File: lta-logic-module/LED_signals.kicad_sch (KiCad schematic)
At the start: 12 parts, among them J3 Conn_01x12, J4 Conn_01x12, U10 SN74LVC00AD, U6 SN74LVC00AD, U7 SN74LVC00AD, U9 SN74LVC00AD

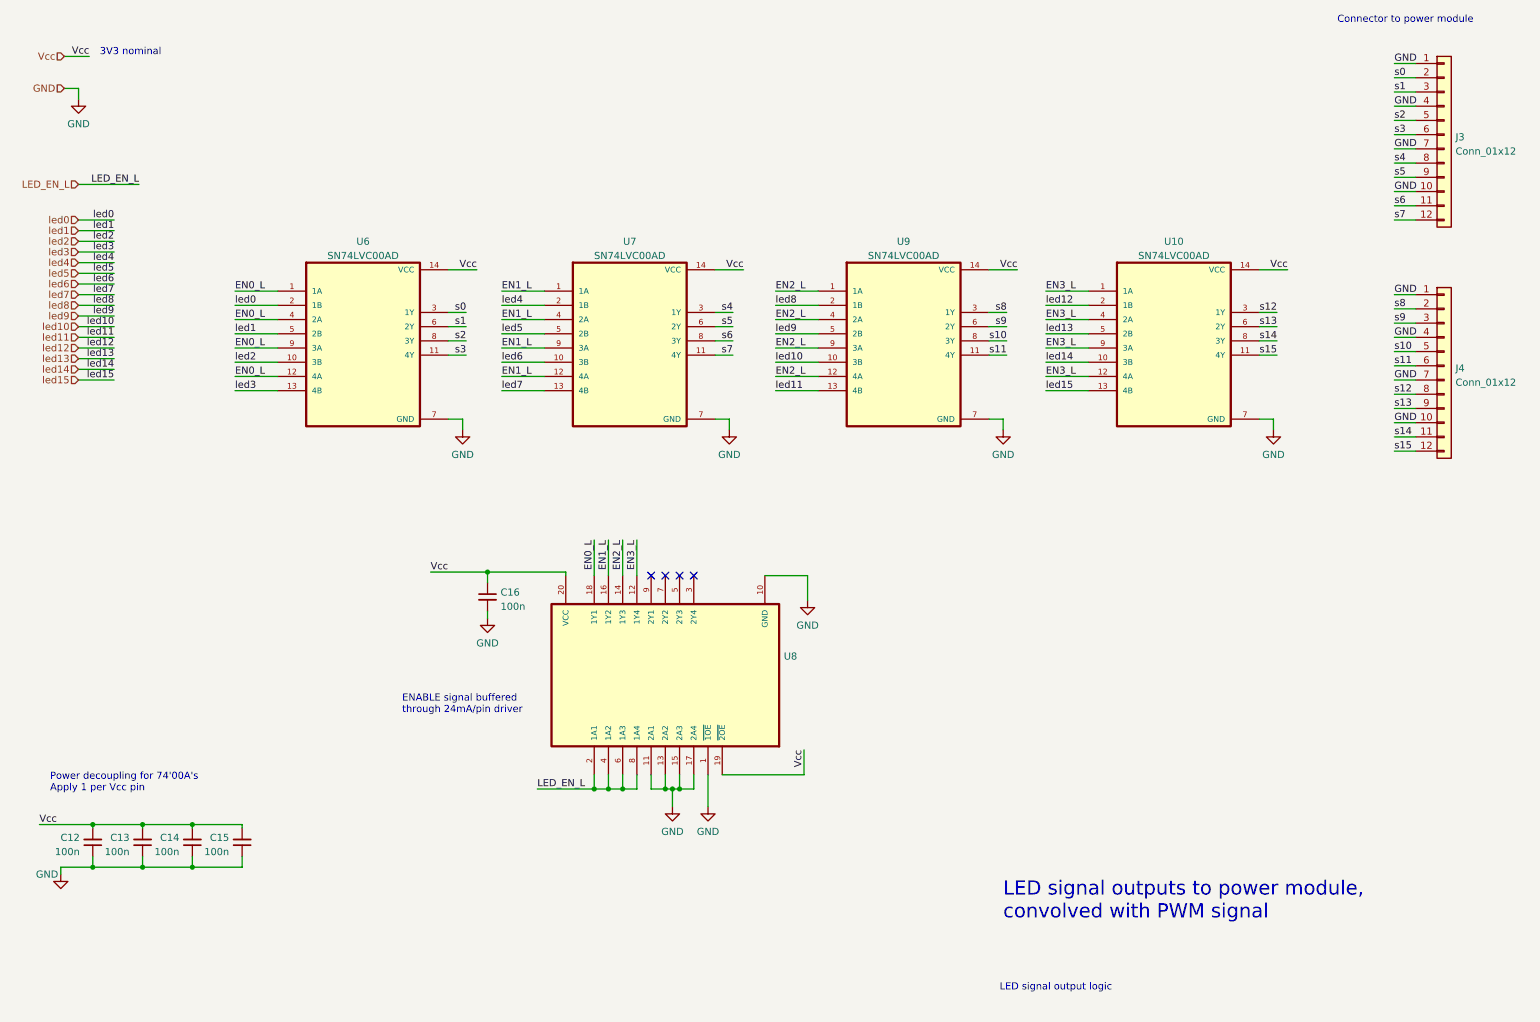
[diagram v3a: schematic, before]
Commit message: Add light sensor circuit.
Adjust TODOs and comments after testing btn circuit.
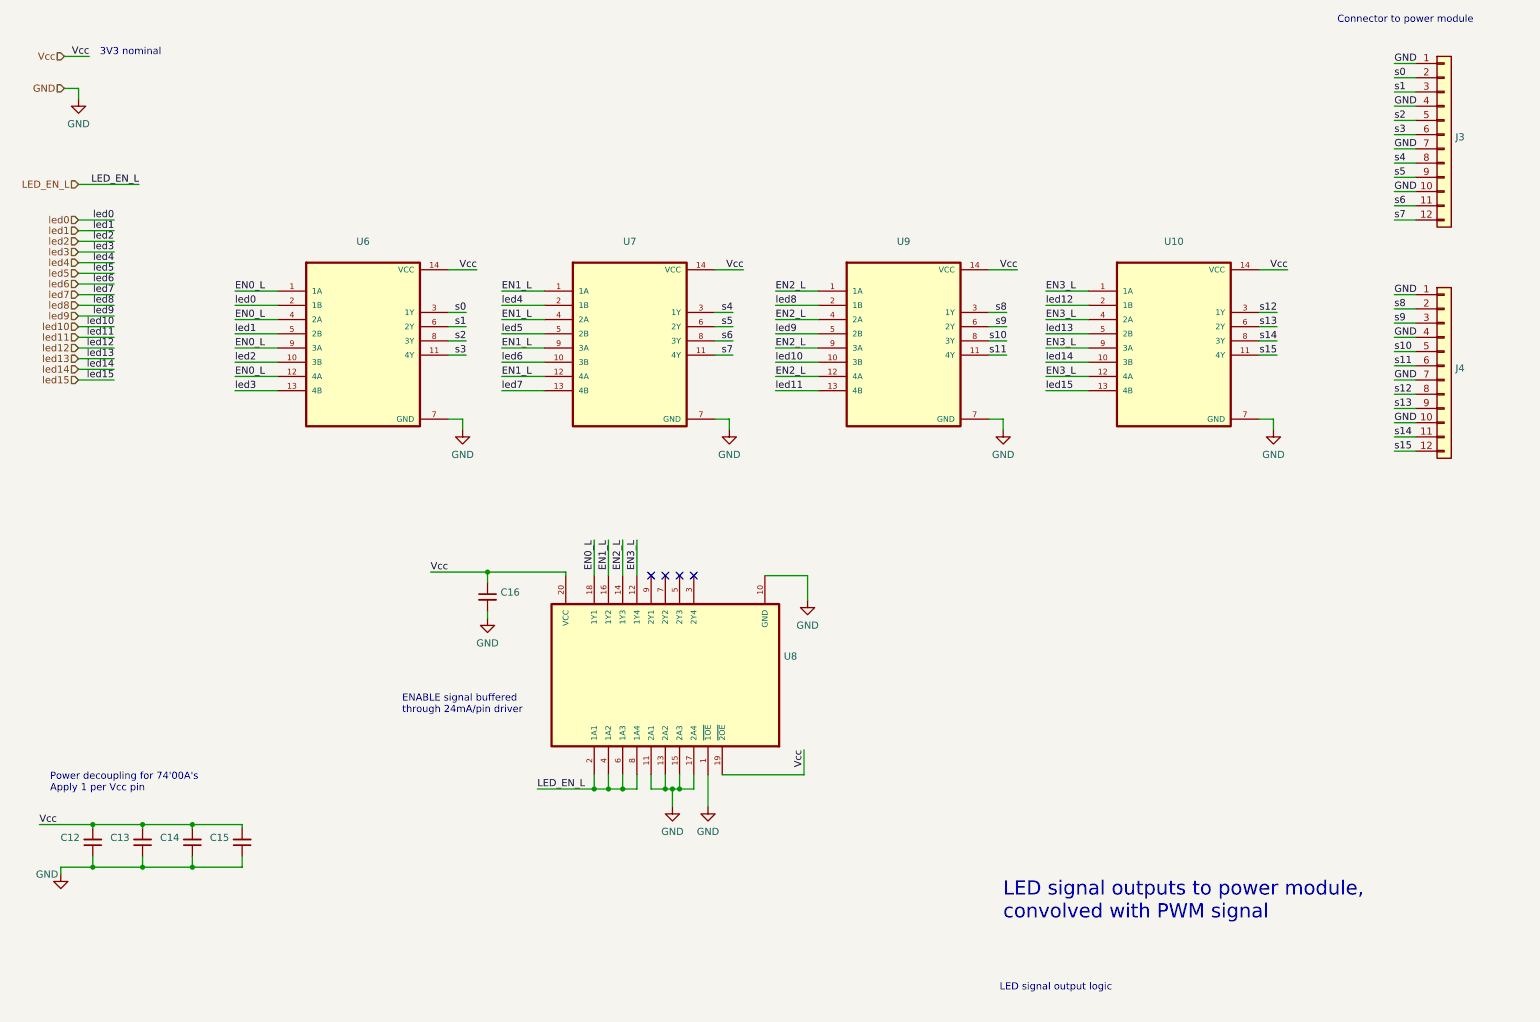
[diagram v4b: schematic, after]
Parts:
- C12, C13, C14, C15, C16: value 100n -> (none); footprint Capacitor_SMD:C_0603_1608Metric -> (none)
- J3, J4: value Conn_01x12 -> (none); footprint Connector_PinHeader_2.54mm:PinHeader_1x12_P2.54mm_Vertical -> (none)
- U10, U6, U7, U9: value SN74LVC00AD -> (none); footprint Aaron_TI_Parts:TI_SOIC_D_R-PDSO-G14 -> (none)
- U8: footprint Aaron_TI_Parts:TI_SOIC_DW0020A -> (none)
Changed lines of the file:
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@@
       (effects (font (size 1.27 1.27)) (justify right))
     )
-    (property "Value" "100n" (id 1) (at 26.2509 165.5258 0)
-      (effects (font (size 1.27 1.27)) (justify right))
-    )
-    (property "Footprint" "Capacitor_SMD:C_0603_1608Metric" (id 2) (at 28.575 163.83 0)
+    (property "Value" "" (id 1) (at 26.2509 165.5258 0)
+      (effects (font (size 1.27 1.27)) (justify right))
+    )
+    (property "Footprint" "" (id 2) (at 28.575 163.83 0)
       (effects (font (size 1.27 1.27)) hide)
     )
@@
   (symbol (lib_id "power:GND") (at 191.135 90.17 0) (unit 1)
     (in_bom yes) (on_board yes) (fields_autoplaced)
-    (property "Reference" "#PWR040" (id 0) (at 191.135 96.52 0)
+    (property "Reference" "#PWR042" (id 0) (at 191.135 96.52 0)
       (effects (font (size 1.27 1.27)) hide)
     )
@@
     (in_bom yes) (on_board yes) (fields_autoplaced)
     (property "Reference" "U6" (id 0) (at 76.835 56.549 0))
-    (property "Value" "SN74LVC00AD" (id 1) (at 76.835 59.0859 0))
-    (property "Footprint" "Aaron_TI_Parts:TI_SOIC_D_R-PDSO-G14" (id 2) (at 74.295 80.645 0)
+    (property "Value" "" (id 1) (at 76.835 59.0859 0))
+    (property "Footprint" "" (id 2) (at 74.295 80.645 0)
       (effects (font (size 1.27 1.27)) (justify left bottom) hide)
     )
@@
       (effects (font (size 1.27 1.27)) (justify right))
     )
-    (property "Value" "100n" (id 1) (at 52.9209 165.5258 0)
-      (effects (font (size 1.27 1.27)) (justify right))
-    )
-    (property "Footprint" "Capacitor_SMD:C_0603_1608Metric" (id 2) (at 55.245 163.83 0)
+    (property "Value" "" (id 1) (at 52.9209 165.5258 0)
+      (effects (font (size 1.27 1.27)) (justify right))
+    )
+    (property "Footprint" "" (id 2) (at 55.245 163.83 0)
       (effects (font (size 1.27 1.27)) hide)
     )
@@
       (effects (font (size 1.27 1.27)) (justify left))
     )
-    (property "Value" "Conn_01x12" (id 1) (at 271.907 40.4372 0)
-      (effects (font (size 1.27 1.27)) (justify left))
-    )
-    (property "Footprint" "Connector_PinHeader_2.54mm:PinHeader_1x12_P2.54mm_Vertical" (id 2) (at 269.875 37.465 0)
+    (property "Value" "" (id 1) (at 271.907 40.4372 0)
+      (effects (font (size 1.27 1.27)) (justify left))
+    )
+    (property "Footprint" "" (id 2) (at 269.875 37.465 0)
       (effects (font (size 1.27 1.27)) hide)
     )
@@
     (in_bom yes) (on_board yes) (fields_autoplaced)
     (property "Reference" "U10" (id 0) (at 221.615 56.549 0))
-    (property "Value" "SN74LVC00AD" (id 1) (at 221.615 59.0859 0))
-    (property "Footprint" "Aaron_TI_Parts:TI_SOIC_D_R-PDSO-G14" (id 2) (at 219.075 80.645 0)
+    (property "Value" "" (id 1) (at 221.615 59.0859 0))
+    (property "Footprint" "" (id 2) (at 219.075 80.645 0)
       (effects (font (size 1.27 1.27)) (justify left bottom) hide)
     )
@@
   (symbol (lib_id "power:GND") (at 22.86 169.545 0) (unit 1)
     (in_bom yes) (on_board yes)
-    (property "Reference" "#PWR032" (id 0) (at 22.86 175.895 0)
+    (property "Reference" "#PWR034" (id 0) (at 22.86 175.895 0)
       (effects (font (size 1.27 1.27)) hide)
     )
@@
   (symbol (lib_id "power:GND") (at 239.395 90.17 0) (unit 1)
     (in_bom yes) (on_board yes) (fields_autoplaced)
-    (property "Reference" "#PWR041" (id 0) (at 239.395 96.52 0)
+    (property "Reference" "#PWR043" (id 0) (at 239.395 96.52 0)
       (effects (font (size 1.27 1.27)) hide)
     )
@@
       (effects (font (size 1.27 1.27)) (justify left))
     )
-    (property "Value" "100n" (id 1) (at 101.3841 121.7235 0)
-      (effects (font (size 1.27 1.27)) (justify left))
-    )
-    (property "Footprint" "Capacitor_SMD:C_0603_1608Metric" (id 2) (at 99.06 120.015 0)
+    (property "Value" "" (id 1) (at 101.3841 121.7235 0)
+      (effects (font (size 1.27 1.27)) (justify left))
+    )
+    (property "Footprint" "" (id 2) (at 99.06 120.015 0)
       (effects (font (size 1.27 1.27)) hide)
     )
@@
       (effects (font (size 1.27 1.27)) (justify right))
     )
-    (property "Value" "100n" (id 1) (at 35.1409 165.5258 0)
-      (effects (font (size 1.27 1.27)) (justify right))
-    )
-    (property "Footprint" "Capacitor_SMD:C_0603_1608Metric" (id 2) (at 37.465 163.83 0)
+    (property "Value" "" (id 1) (at 35.1409 165.5258 0)
+      (effects (font (size 1.27 1.27)) (justify right))
+    )
+    (property "Footprint" "" (id 2) (at 37.465 163.83 0)
       (effects (font (size 1.27 1.27)) hide)
     )
@@
     (in_bom yes) (on_board yes) (fields_autoplaced)
     (property "Reference" "U7" (id 0) (at 124.46 56.549 0))
-    (property "Value" "SN74LVC00AD" (id 1) (at 124.46 59.0859 0))
-    (property "Footprint" "Aaron_TI_Parts:TI_SOIC_D_R-PDSO-G14" (id 2) (at 121.92 80.645 0)
+    (property "Value" "" (id 1) (at 124.46 59.0859 0))
+    (property "Footprint" "" (id 2) (at 121.92 80.645 0)
       (effects (font (size 1.27 1.27)) (justify left bottom) hide)
     )
@@
       (effects (font (size 1.27 1.27)) (justify right))
     )
-    (property "Footprint" "Aaron_TI_Parts:TI_SOIC_DW0020A" (id 2) (at 130.81 133.985 0)
+    (property "Footprint" "" (id 2) (at 130.81 133.985 0)
       (effects (font (size 1.27 1.27)) (justify left bottom) hide)
     )
@@
   (symbol (lib_id "power:GND") (at 156.21 120.65 0) (unit 1)
     (in_bom yes) (on_board yes) (fields_autoplaced)
-    (property "Reference" "#PWR039" (id 0) (at 156.21 127 0)
+    (property "Reference" "#PWR041" (id 0) (at 156.21 127 0)
       (effects (font (size 1.27 1.27)) hide)
     )
@@
   (symbol (lib_id "power:GND") (at 99.06 123.825 0) (unit 1)
     (in_bom yes) (on_board yes) (fields_autoplaced)
-    (property "Reference" "#PWR035" (id 0) (at 99.06 130.175 0)
+    (property "Reference" "#PWR037" (id 0) (at 99.06 130.175 0)
       (effects (font (size 1.27 1.27)) hide)
     )
@@
   (symbol (lib_id "power:GND") (at 142.24 90.17 0) (unit 1)
     (in_bom yes) (on_board yes) (fields_autoplaced)
-    (property "Reference" "#PWR038" (id 0) (at 142.24 96.52 0)
+    (property "Reference" "#PWR040" (id 0) (at 142.24 96.52 0)
       (effects (font (size 1.27 1.27)) hide)
     )
@@
       (effects (font (size 1.27 1.27)) (justify right))
     )
-    (property "Value" "100n" (id 1) (at 44.0309 165.5258 0)
-      (effects (font (size 1.27 1.27)) (justify right))
-    )
-    (property "Footprint" "Capacitor_SMD:C_0603_1608Metric" (id 2) (at 46.355 163.83 0)
+    (property "Value" "" (id 1) (at 44.0309 165.5258 0)
+      (effects (font (size 1.27 1.27)) (justify right))
+    )
+    (property "Footprint" "" (id 2) (at 46.355 163.83 0)
       (effects (font (size 1.27 1.27)) hide)
     )
@@
   (symbol (lib_id "power:GND") (at 132.08 157.48 0) (unit 1)
     (in_bom yes) (on_board yes) (fields_autoplaced)
-    (property "Reference" "#PWR036" (id 0) (at 132.08 163.83 0)
+    (property "Reference" "#PWR038" (id 0) (at 132.08 163.83 0)
       (effects (font (size 1.27 1.27)) hide)
     )
@@
   (symbol (lib_id "power:GND") (at 138.43 157.48 0) (unit 1)
     (in_bom yes) (on_board yes) (fields_autoplaced)
-    (property "Reference" "#PWR037" (id 0) (at 138.43 163.83 0)
+    (property "Reference" "#PWR039" (id 0) (at 138.43 163.83 0)
       (effects (font (size 1.27 1.27)) hide)
     )
@@
     (in_bom yes) (on_board yes) (fields_autoplaced)
     (property "Reference" "U9" (id 0) (at 173.355 56.549 0))
-    (property "Value" "SN74LVC00AD" (id 1) (at 173.355 59.0859 0))
-    (property "Footprint" "Aaron_TI_Parts:TI_SOIC_D_R-PDSO-G14" (id 2) (at 170.815 80.645 0)
+    (property "Value" "" (id 1) (at 173.355 59.0859 0))
+    (property "Footprint" "" (id 2) (at 170.815 80.645 0)
       (effects (font (size 1.27 1.27)) (justify left bottom) hide)
     )
@@
   (symbol (lib_id "power:GND") (at 26.035 31.115 0) (unit 1)
     (in_bom yes) (on_board yes) (fields_autoplaced)
-    (property "Reference" "#PWR033" (id 0) (at 26.035 37.465 0)
+    (property "Reference" "#PWR035" (id 0) (at 26.035 37.465 0)
       (effects (font (size 1.27 1.27)) hide)
     )
@@
   (symbol (lib_id "power:GND") (at 94.615 90.17 0) (unit 1)
     (in_bom yes) (on_board yes) (fields_autoplaced)
-    (property "Reference" "#PWR034" (id 0) (at 94.615 96.52 0)
+    (property "Reference" "#PWR036" (id 0) (at 94.615 96.52 0)
       (effects (font (size 1.27 1.27)) hide)
     )
@@
       (effects (font (size 1.27 1.27)) (justify left))
     )
-    (property "Value" "Conn_01x12" (id 1) (at 271.907 81.7122 0)
-      (effects (font (size 1.27 1.27)) (justify left))
-    )
-    (property "Footprint" "Connector_PinHeader_2.54mm:PinHeader_1x12_P2.54mm_Vertical" (id 2) (at 269.875 78.74 0)
-      (effects (font (size 1.27 1.27)) hide)
-    )
+    (property "Value" "" (id 1) (at 271.907 81.7122 0)
+      (effects (font (size 1.27 1.27)) (justify left))
+    )
+    (property "Footprint" "" (id 2) (at 269.875 78.74 0)
+      (effects (font (size 1.27 1.27)) hide)
+    )

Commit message: Add main draft of PCB layout for logic module.
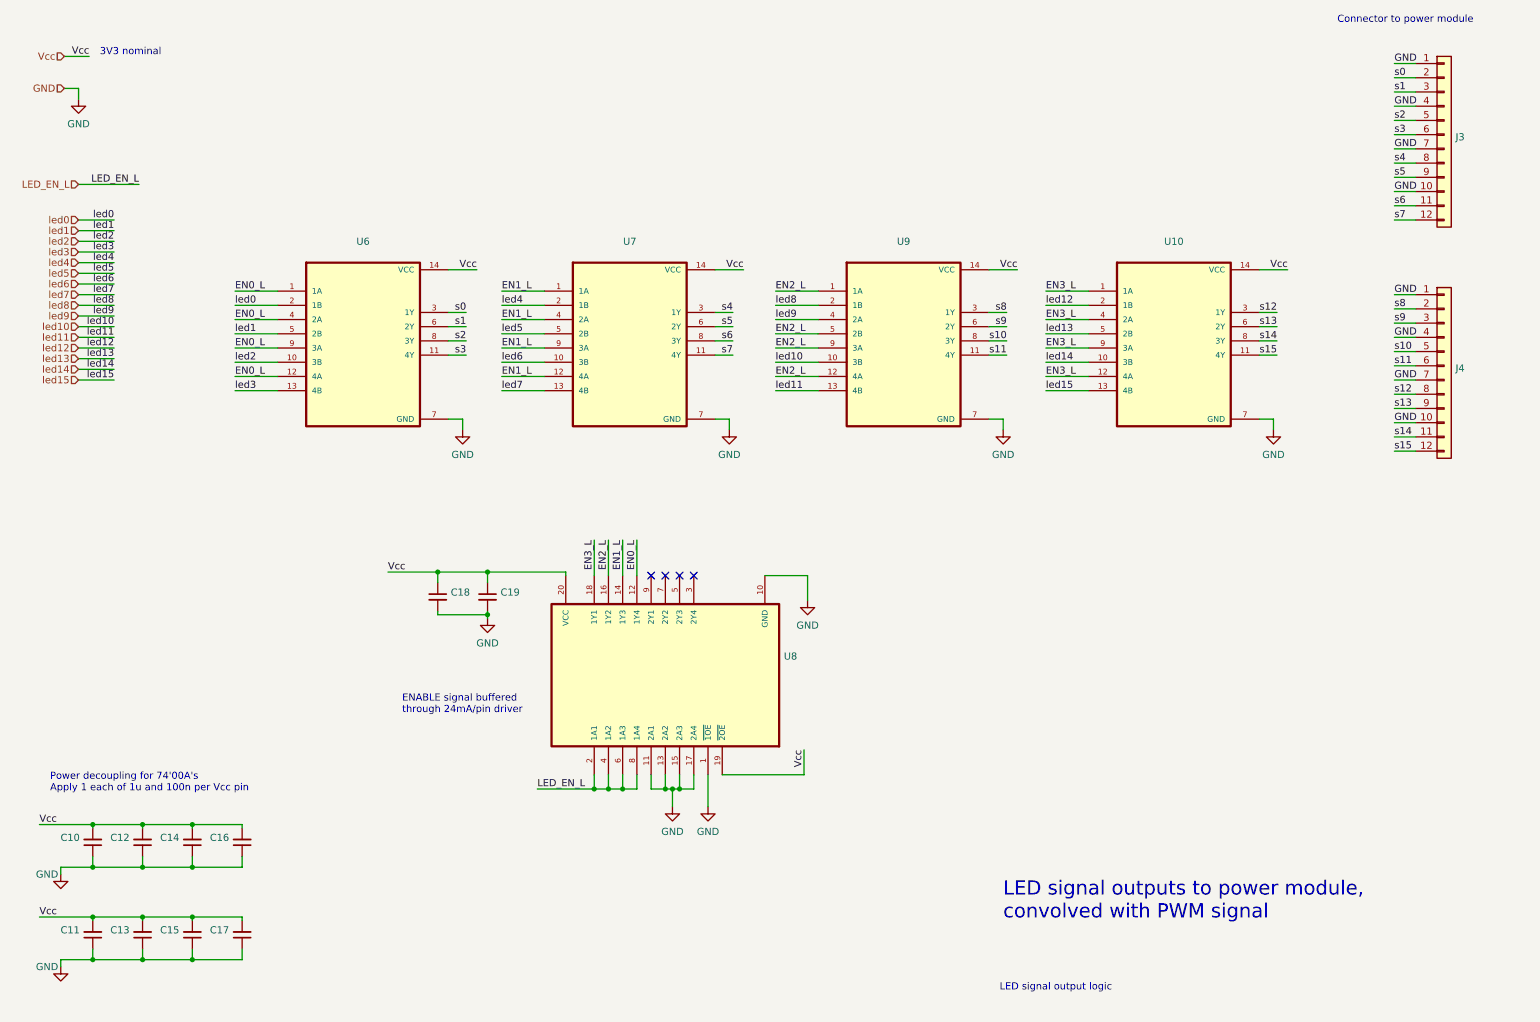
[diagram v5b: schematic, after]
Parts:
- added C11, C13, C15, C17, C18: (no value), symbol Device:C_Small
- U10, U6, U7, U9: Comment (none) -> Exact MFR/MPN required
- U8: Comment (none) -> Exact MFR/MPN required; -ADW or -ADWR packaging OK.
- renumbered C12 to C10, C13 to C12, C15 to C16, C16 to C19
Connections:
- net EN0_L: now also U8.12 (1Y4); no longer U8.18 (1Y1)
- net EN1_L: now also U8.14 (1Y3); no longer U8.16 (1Y2)
- net EN2_L: now also U8.16 (1Y2), U9.5 (2B); no longer U8.14 (1Y3), U9.4 (2A)
- net EN3_L: now also U8.18 (1Y1); no longer U8.12 (1Y4)
- net GND: now also C11.1, C13.1, C15.1, C17.1, C18.2
- net Vcc: now also C11.2, C13.2, C15.2, C17.2, C18.1
- net led9: now also U9.4 (2A); no longer U9.5 (2B)
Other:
- note added: "Power decoupling for 74'00A's Apply 1 each of 1u and 100n per Vcc pin"
- note removed: "Power decoupling for 74'00A's Apply 1 per Vcc pin"
